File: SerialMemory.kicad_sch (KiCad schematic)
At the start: 0 parts

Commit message: 3/8/2025
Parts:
- added C20, C21: 22 uF, Capacitor_SMD:C_1206_3216Metric, symbol Device:C
- added C22, C23, C24: 100 nF, Capacitor_SMD:C_0603_1608Metric, symbol Device:C
- added D7: PUSB3AB4Z, jka_library:SON50P100X250X50-10N, symbol jka_library:PUSB3AB4Z
- added D8: ESD5Zxx, Diode_SMD:D_SOD-523, symbol Diode:ESD5Zxx
- added J6: Micro_SD_Card, jka_library:GCT_MEM2061-01-188-00-A_REVA, symbol Connector:Micro_SD_Card
- added R24, R25, R26, R27, R28: 10k, Resistor_SMD:R_0603_1608Metric, symbol Device:R_US
- added U4: MX25L12833FM2I, Package_SO:SOP-8_5.28x5.23mm_P1.27mm, symbol jka_library:MX25L12833FM2I
- added U5: CAT24C256, Package_SO:SOIC-8_3.9x4.9mm_P1.27mm, symbol Memory_EEPROM:CAT24C256
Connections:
- new net +3V3: C20.1, C21.1, C22.1, C23.1, C24.1, D8.1 (K), J6.4 (VDD), R24.1, R25.2, R26.1, R27.1, R28.2, U4.8 (VCC), U5.8 (VCC)
- new net DAT1: J6.8 (DAT1), R28.1
- new net DAT2: J6.1 (DAT2), R27.2
- new net EEPROM_WP: U5.7 (WP)
- new net GND: C20.2, C21.2, C22.2, C23.2, C24.2, D7.3 (GND_1), D7.8 (GND_2), D8.2 (A), J6.6 (VSS), J6.9 (SHIELD), U4.4 (GND), U5.1 (A0), U5.2 (A1), U5.3 (A2), U5.4 (GND)
- new net I2C_SCL: U5.6 (SCL)
- new net I2C_SDA: U5.5 (SDA)
- new net QSPI_CLK: U4.6 (SCLK)
- new net QSPI_FLASH_CS: R24.2, U4.1 (~{CS})
- new net QSPI_SIO0: U4.5 (SI/SIO0)
- new net QSPI_SIO1: U4.2 (SO/SIO1)
- new net QSPI_SIO2: U4.3 (~{WP}/SIO2)
- new net QSPI_SIO3: U4.7 (~{HOLD}/SIO3)
- new net SPI_CLK: D7.2 (CH2), J6.5 (CLK)
- new net SPI_DI: D7.4 (CH3), J6.3 (CMD)
- new net SPI_DO: D7.1 (CH1), J6.7 (DAT0), R25.1
- new net SPI_SD_CS: D7.5 (CH4), J6.2 (DAT3/CD), R26.2
- no-connect marks 0 -> 4
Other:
- note added: "16 MB NOR Flash"
- note added: "32 KB EEPROM"
- note added: "Addr: 1010 000"
- note added: "ESD protection"
- note added: "Micro SD"

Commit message: Layout draft complete
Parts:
- added D15, D9: ESD5Zxx, Diode_SMD:D_SOD-523, symbol Diode:ESD5Zxx
- added R50: 22R, Resistor_SMD:R_0603_1608Metric, symbol Device:R_US
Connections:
- net DAT1: now also D9.1 (K)
- net DAT2: now also D15.1 (K)
- net GND: now also D15.2 (A), D9.2 (A)
- net QSPI_CLK: now also R50.1; no longer U4.6 (SCLK)
- net QSPI_FLASH_CS renamed QSPI_NCS
- net QSPI_SIO0 renamed QSPI_IO0
- net QSPI_SIO1 renamed QSPI_IO1
- net QSPI_SIO2 renamed QSPI_IO2
- net QSPI_SIO3 renamed QSPI_IO3
- net SPI_CLK renamed SPI2_SCK
- net SPI_DI renamed SPI2_MOSI
- net SPI_DO renamed SPI2_MISO
- net SPI_SD_CS renamed SPI2_NSS
- new net QSPI_CLK_PIN: R50.2, U4.6 (SCLK)
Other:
- note added: "ALT: MX25L12833FZNI-10G"
- title: (none) -> Jakka1
- moved on the sheet: D7, R24

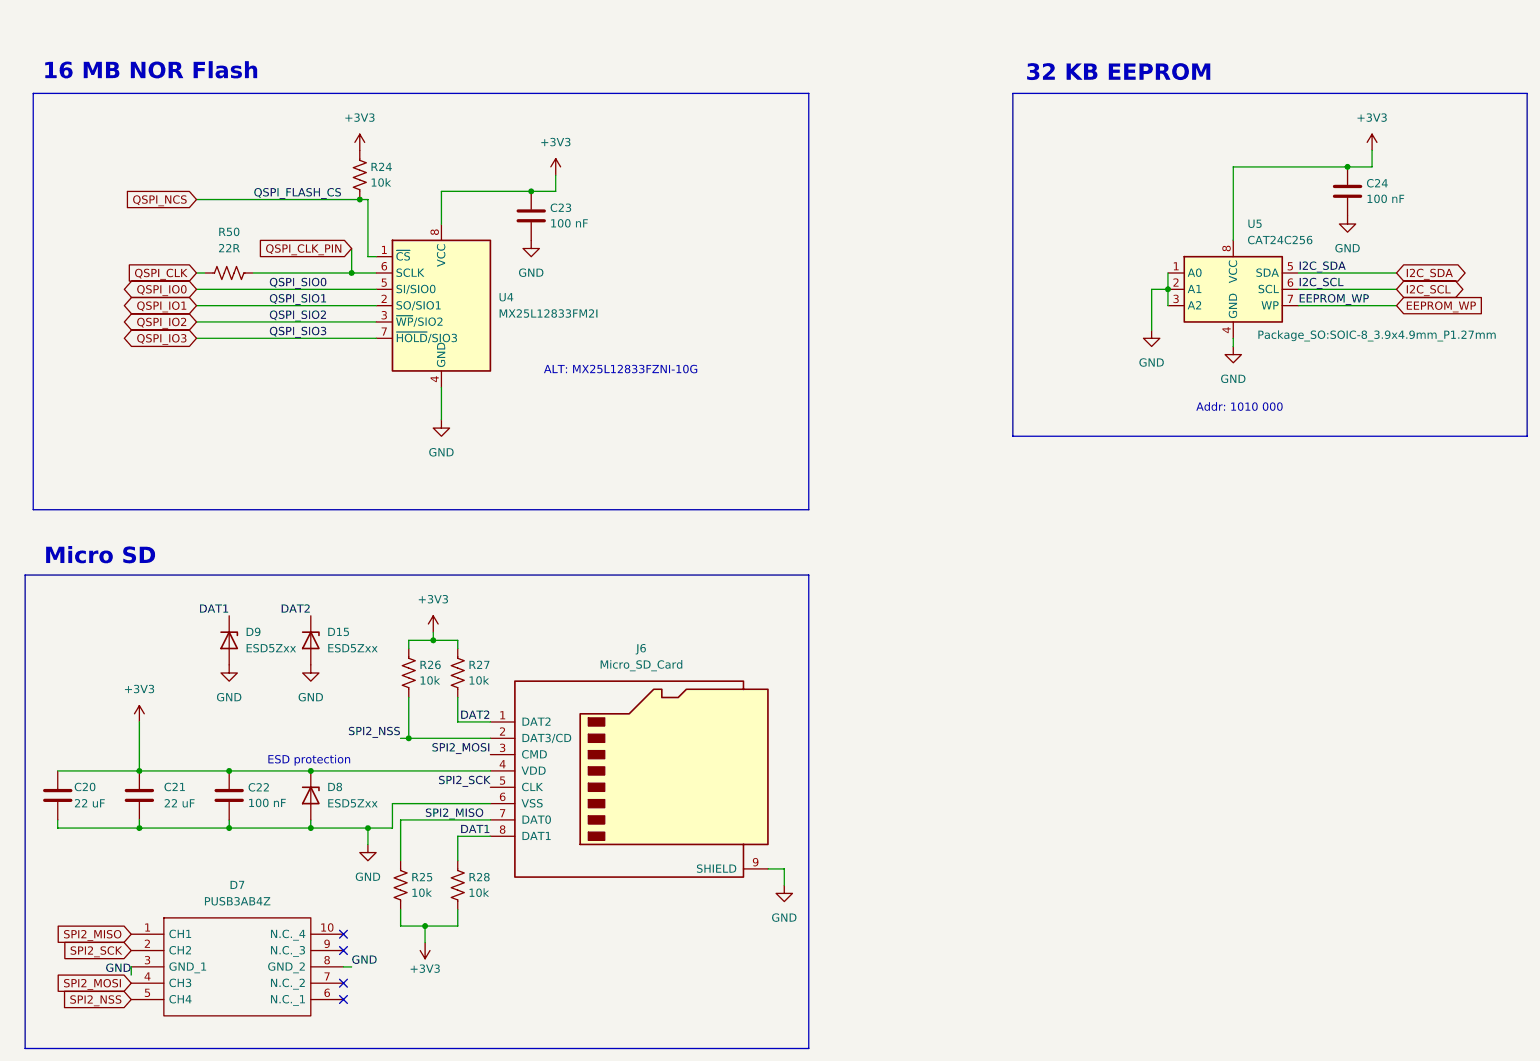
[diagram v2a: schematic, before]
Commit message: First draft of design output, schematic, and layout complete
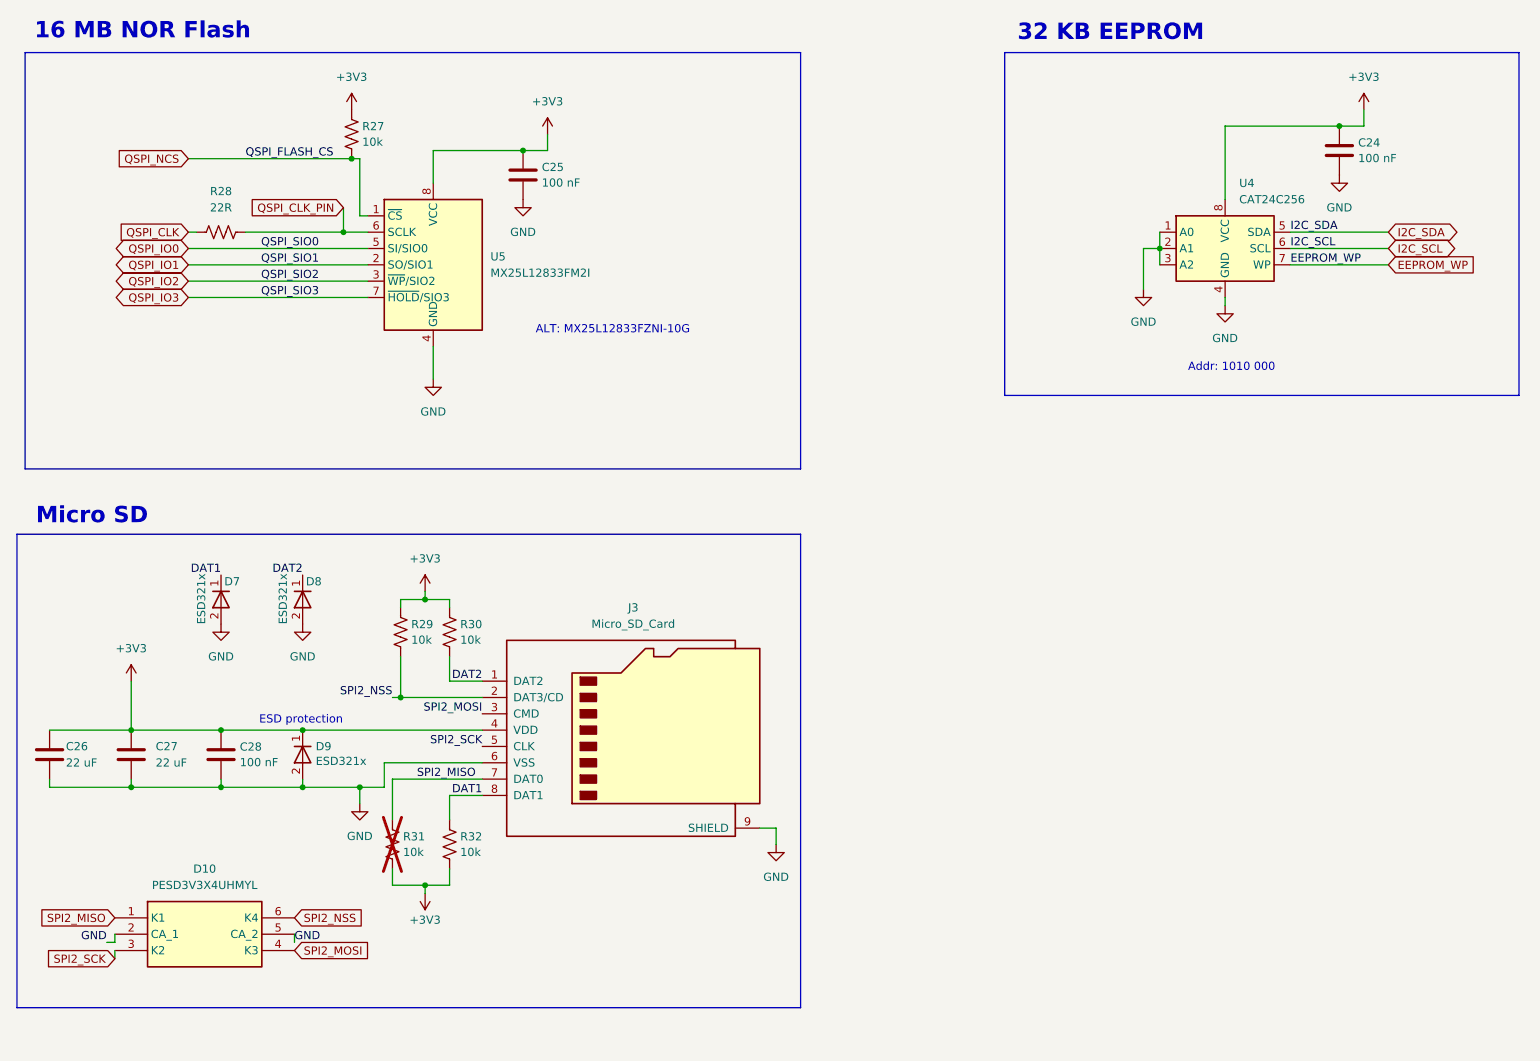
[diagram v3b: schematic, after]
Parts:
- removed D15, D8, D9: ESD5Zxx, Diode_SMD:D_SOD-523, symbol Diode:ESD5Zxx
- removed D7: PUSB3AB4Z, jka_library:SON50P100X250X50-10N, symbol jka_library:PUSB3AB4Z
- added D10: PESD3V3X4UHMYL, jka_library:SON45P80X130X43-6N, symbol jka_library:PESD3V3X4UHMYL
- added D7, D8, D9: ESD321x, jka_library:SODFL1608X77N, symbol jka_library:ESD321DYAR
- R31: renamed from R25; now not fitted
- renumbered C23 to C25, C20 to C26, C21 to C27, C22 to C28, J6 to J3, R24 to R27, R50 to R28, R26 to R29, R27 to R30, R28 to R32, U5 to U4, U4 to U5
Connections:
- net +3V3: now also D9.1 (K)
- net DAT1: now also D7.1 (K)
- net DAT2: now also D8.1 (K)
- net GND: now also D10.2 (CA_1), D10.5 (CA_2), D7.2 (A), D8.2 (A), D9.2 (A)
- net SPI2_MISO: now also D10.1 (K1)
- net SPI2_MOSI: now also D10.4 (K3)
- net SPI2_NSS: now also D10.6 (K4)
- net SPI2_SCK: now also D10.3 (K2)
- no-connect marks 4 -> 0
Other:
- company: (none) -> Jacob Kapala
- moved on the sheet: C24, C25, C26, C27, C28, J3, R27, R28, R29, R30, R32, U4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
